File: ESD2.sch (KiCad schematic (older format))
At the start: 3 parts, among them U4 USBLC6-2SC6, U5 USBLC6-2SC6

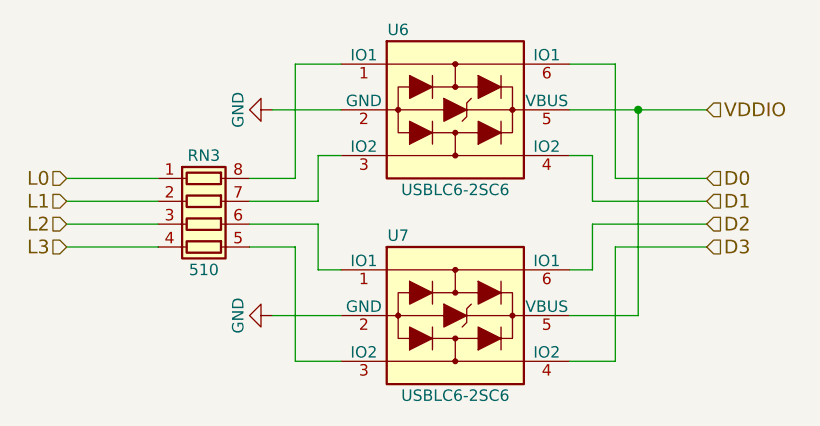
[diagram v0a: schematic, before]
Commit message: Changing the power delivery subsystem.
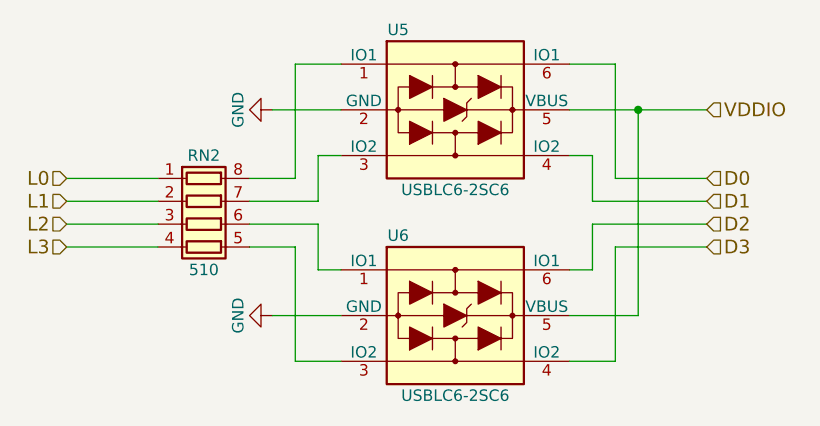
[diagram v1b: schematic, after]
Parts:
- renumbered U4 to U5, U5 to U6
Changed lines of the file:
@@
 LIBS:zetex
 LIBS:Zilog
+LIBS:DAP42-cache
 EELAYER 25 0
 EELAYER END
@@
 $EndDescr
 $Comp
-L USBLC6-2SC6 U5
+L USBLC6-2SC6 U6
 U 1 1 59FAE714
 P 5900 4200
-AR Path="/59FAE697/59FAE714" Ref="U5"  Part="1"
-AR Path="/59FB1991/59FAE714" Ref="U7"  Part="1"
-F 0 "U7" H 5650 4550 50  0000 C CNN
+AR Path="/59FAE697/59FAE714" Ref="U6"  Part="1"
+AR Path="/59FB1991/59FAE714" Ref="U8"  Part="1"
+F 0 "U6" H 5650 4550 50  0000 C CNN
 F 1 "USBLC6-2SC6" H 5900 3850 50  0000 C CNN
 F 2 "TO_SOT_Packages_SMD:SOT-23-6_Handsoldering" H 6550 4550 50  0001 C CNN
@@
 AR Path="/59FAE697/59FAE777" Ref="RN2"  Part="1"
 AR Path="/59FB1991/59FAE777" Ref="RN3"  Part="1"
-F 0 "RN3" V 4500 3800 50  0000 C CNN
+F 0 "RN2" V 4500 3800 50  0000 C CNN
 F 1 "510" V 5000 3800 50  0000 C CNN
 F 2 "Resistors_SMD:R_Array_Convex_4x0603" V 5075 3800 50  0001 C CNN
@@
 	4200 3700 4600 3700
 $Comp
-L USBLC6-2SC6 U4
+L USBLC6-2SC6 U5
 U 1 1 59FAE952
 P 5900 3300
-AR Path="/59FAE697/59FAE952" Ref="U4"  Part="1"
-AR Path="/59FB1991/59FAE952" Ref="U6"  Part="1"
-F 0 "U6" H 5650 3650 50  0000 C CNN
+AR Path="/59FAE697/59FAE952" Ref="U5"  Part="1"
+AR Path="/59FB1991/59FAE952" Ref="U7"  Part="1"
+F 0 "U5" H 5650 3650 50  0000 C CNN
 F 1 "USBLC6-2SC6" H 5900 2950 50  0000 C CNN
 F 2 "TO_SOT_Packages_SMD:SOT-23-6_Handsoldering" H 6550 3650 50  0001 C CNN
@@
 	6600 3900 7000 3900
 $Comp
-L GND #PWR025
+L GND #PWR026
 U 1 1 59FAEA37
 P 5100 3300
-AR Path="/59FAE697/59FAEA37" Ref="#PWR025"  Part="1"
-AR Path="/59FB1991/59FAEA37" Ref="#PWR027"  Part="1"
-F 0 "#PWR027" H 5100 3050 50  0001 C CNN
+AR Path="/59FAE697/59FAEA37" Ref="#PWR026"  Part="1"
+AR Path="/59FB1991/59FAEA37" Ref="#PWR028"  Part="1"
+F 0 "#PWR028" H 5100 3050 50  0001 C CNN
 F 1 "GND" H 5100 3150 50  0000 C CNN
 F 2 "" H 5100 3300 50  0001 C CNN
@@
 $EndComp
 $Comp
-L GND #PWR026
+L GND #PWR027
 U 1 1 59FAEA54
 P 5100 4200
-AR Path="/59FAE697/59FAEA54" Ref="#PWR026"  Part="1"
-AR Path="/59FB1991/59FAEA54" Ref="#PWR028"  Part="1"
-F 0 "#PWR028" H 5100 3950 50  0001 C CNN
+AR Path="/59FAE697/59FAEA54" Ref="#PWR027"  Part="1"
+AR Path="/59FB1991/59FAEA54" Ref="#PWR029"  Part="1"
+F 0 "#PWR029" H 5100 3950 50  0001 C CNN
 F 1 "GND" H 5100 4050 50  0000 C CNN
 F 2 "" H 5100 4200 50  0001 C CNN
